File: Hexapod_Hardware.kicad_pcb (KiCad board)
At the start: 4 copper layers, 92.2 x 72.1 mm, 107 parts, among them IC1 MCP3008-I_SL, IC2 MCP3008-I_SL, IC3 MCP3008-I_SL, IC4 STM32G030K8T6, J1 Conn_01x05_Pin, J10 Conn_01x03_Female, J11 Conn_01x03_Female, J12 Conn_01x03_Female, J13 Conn_01x03_Female, J14 Conn_01x03_Female, J15 Conn_01x04_MountingPin, J16 Conn_01x04_MountingPin, J17 Conn_01x04_MountingPin, J18 Screw_Terminal_01x02, J19 Screw_Terminal_01x02, J2 Conn_01x04_Socket, J20 Conn_01x04_Pin, J21 Conn_01x04_Pin, J22 Conn_01x07, J23 Conn_01x03, J3 Conn_01x03_Female, J4 Conn_01x03_Female, J5 Conn_01x03_Female, J6 Conn_01x03_Female, J7 Conn_01x03_Female, J8 Conn_01x03_Female, J9 Conn_01x03_Female, U1 Pico, U10 LM2902, U11 LM2902, U2 LM2902, U3 LM2902, U4 LM2902, U5 LM2902, U6 LM2902, U7 LM2902, U8 AZ1117CH-5.0TRG1

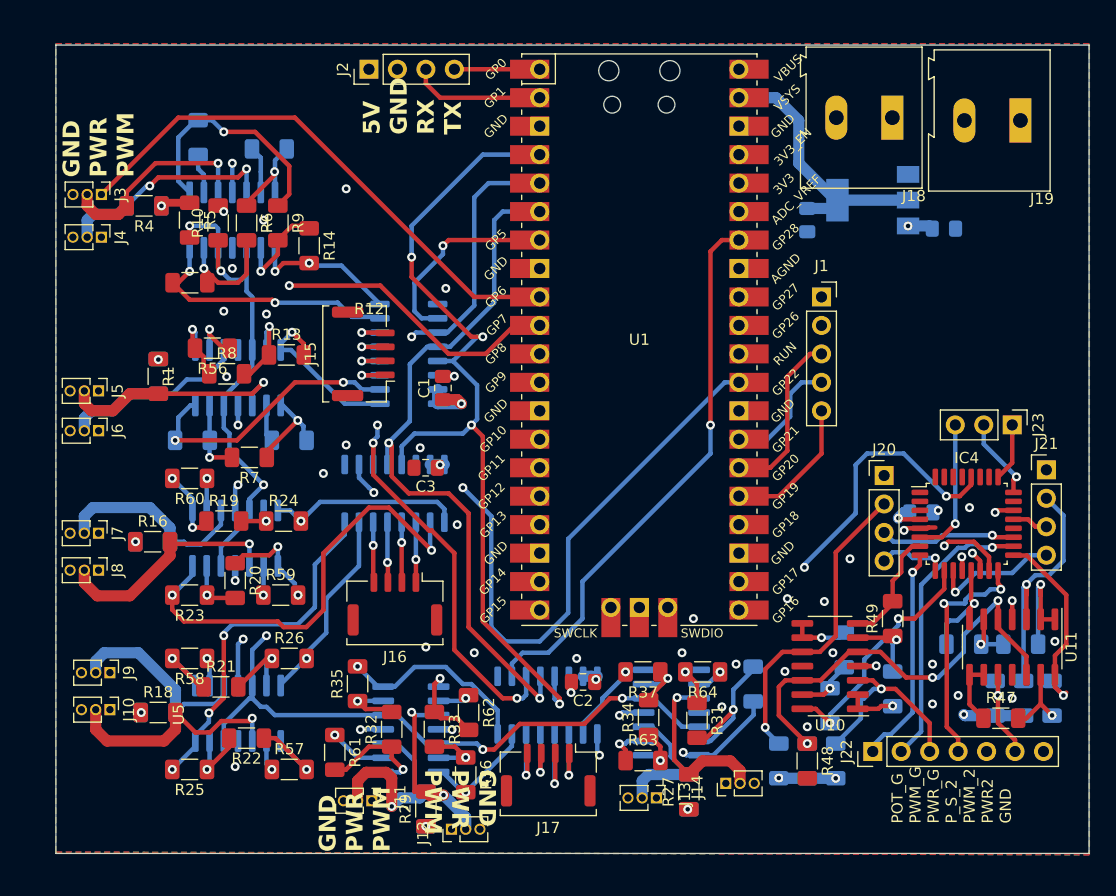
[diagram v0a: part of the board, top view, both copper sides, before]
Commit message: Added testing board + fixed gerber files
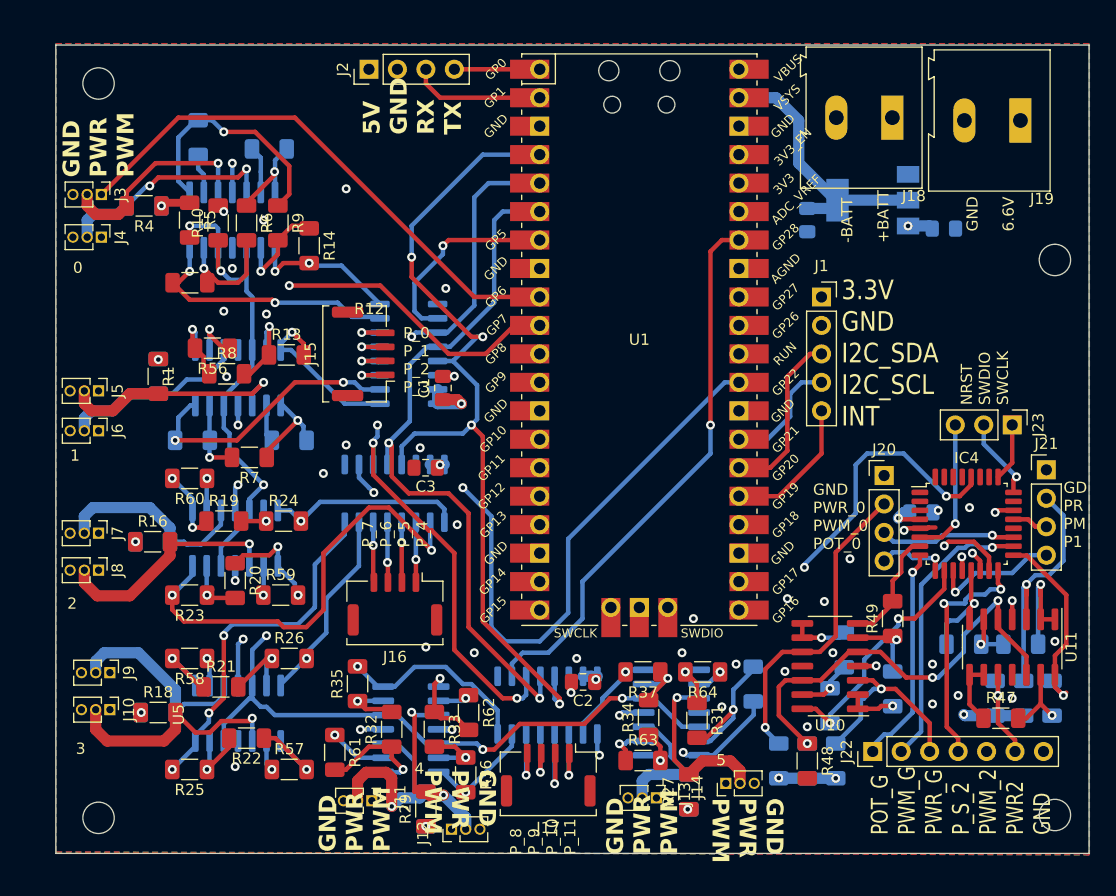
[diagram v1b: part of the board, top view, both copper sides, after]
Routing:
- net +6V: track 209.3 -> 212.5 mm
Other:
- outline, holes or cut-outs redrawn
- board text added: "-BATT +BATT"
- board text added: "0"
- board text added: "1"
- board text added: "2"
- board text added: "3"
- board text added: "3.3V GND I2C_SDA I2C_SCL INT"
- board text added: "4"
- board text added: "5"
- board text added: "GD PR PM P1"
- board text added: "GND 6.6V"
- board text added: "GND PWR_0 PWM_0 POT_0"
- board text added: "NRST SWDIO SWCLK"
- board text added: "P_0 P_1 P_2 P_3"
- board text added: "P_7 P_6 P_5 P_4"
- board text added: "P_8 P_9 P_10 P_11"

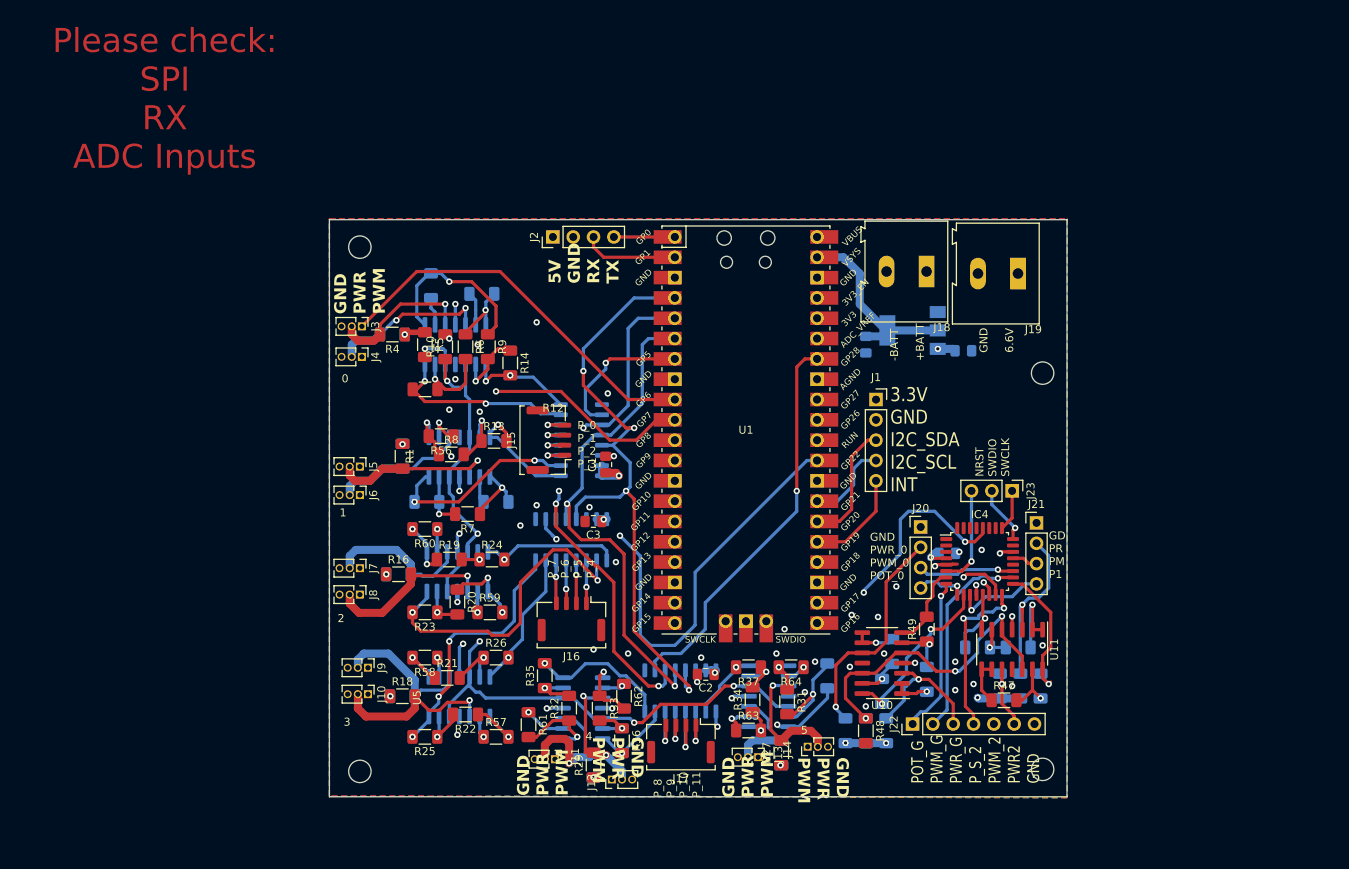
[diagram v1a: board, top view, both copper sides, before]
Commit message: Bord v1.2, added flash memory, changed pinout od servomotor connectors and removed potentiometer signal from servomotors plus one ADC
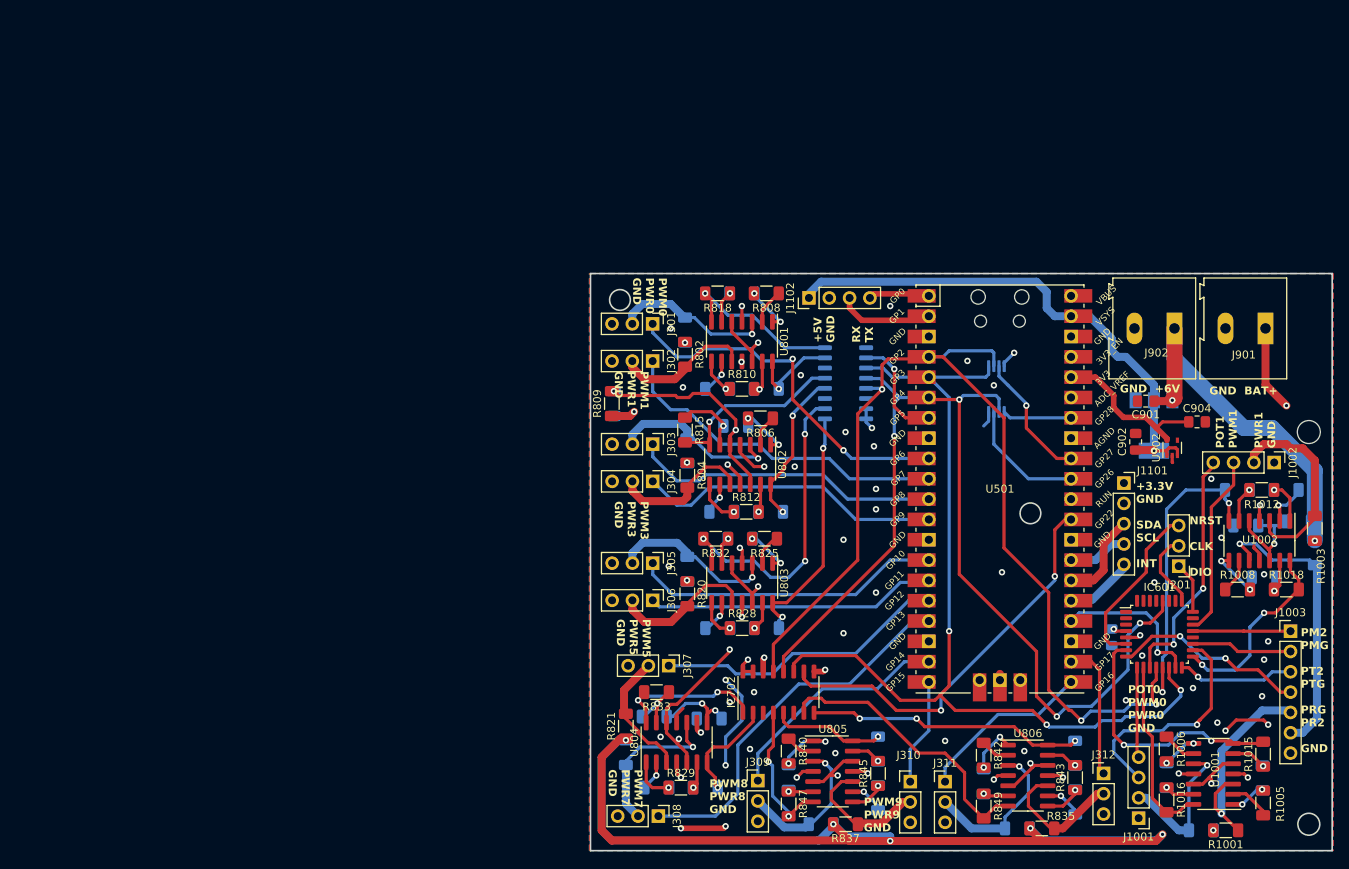
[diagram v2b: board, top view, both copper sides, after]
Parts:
- removed C1, C2, C3: 0,1uF, Capacitor_SMD:C_0805_2012Metric_Pad1.18x1.45mm_HandSolder
- removed C4, C5: 22uF, Capacitor_SMD:C_0805_2012Metric_Pad1.18x1.45mm_HandSolder
- removed C8: 10uF, Capacitor_SMD:C_0805_2012Metric_Pad1.18x1.45mm_HandSolder
- removed IC1, IC2, IC3: MCP3008-I_SL, Package_SO:SO-16_3.9x9.9mm_P1.27mm
- removed IC4: STM32G030K8T6, Package_QFP:LQFP-32_7x7mm_P0.8mm
- removed J1: Conn_01x05_Pin, Connector_PinSocket_2.54mm:PinSocket_1x05_P2.54mm_Vertical
- removed J10, J11, J12, J13, J14, J3, J4, J5, J6, J7, J8, J9: Conn_01x03_Female, Connector_PinHeader_1.27mm:PinHeader_1x03_P1.27mm_Vertical
- removed J15, J16, J17: Conn_01x04_MountingPin, Connector_Molex:Molex_CLIK-Mate_502382-0470_1x04-1MP_P1.25mm_Vertical
- removed J18, J19: Screw_Terminal_01x02, TerminalBlock:TerminalBlock_Altech_AK300-2_P5.00mm
- removed J2: Conn_01x04_Socket, Connector_PinHeader_2.54mm:PinHeader_1x04_P2.54mm_Vertical
- removed J20, J21: Conn_01x04_Pin, Connector_PinHeader_2.54mm:PinHeader_1x04_P2.54mm_Vertical
- removed J22: Conn_01x07, Connector_PinHeader_2.54mm:PinHeader_1x07_P2.54mm_Vertical
- removed J23: Conn_01x03, Connector_PinHeader_2.54mm:PinHeader_1x03_P2.54mm_Vertical
- removed R1, R10, R11, R12, R13, R14, R15, R16, R17, R18, R19, R2, R20, R21, R22, R23, R24, R25, R26, R27, R28, R29, R3, R30, R31, R32, R33, R34, R35, R36, R37, R38, R39, R4, R40, R41, R42, R43, R44, R45, R46, R47, R48, R49, R5, R50, R51, R52, R53, R54, R55, R56, R57, R58, R59, R6, R60, R61, R62, R63, R64, R7, R8, R9: R, Resistor_SMD:R_1206_3216Metric_Pad1.30x1.75mm_HandSolder
- removed U1: Pico, MCU_RaspberryPi_and_Boards:RPi_Pico_SMD_TH
- removed U10, U11, U2, U3, U4, U5, U6, U7: LM2902, Package_SO:SOIC-14_3.9x8.7mm_P1.27mm
- removed U8: AZ1117CH-5.0TRG1, Package_TO_SOT_SMD:SOT-223-3_TabPin2
- added C601: 10uF, Capacitor_SMD:C_0805_2012Metric_Pad1.18x1.45mm_HandSolder, B.Cu at (156.5, 95.2)
- added C901: 22uF, Capacitor_SMD:C_0805_2012Metric_Pad1.18x1.45mm_HandSolder, F.Cu at (160.7, 65.7)
- added C902: 22uF, Capacitor_SMD:C_0805_2012Metric_Pad1.18x1.45mm_HandSolder, F.Cu at (159.5, 70.8)
- added C904: 1uF, Capacitor_SMD:C_0805_2012Metric_Pad1.18x1.45mm_HandSolder, F.Cu at (167.1, 68.3)
- added IC601: STM32G030K8T6, Package_QFP:LQFP-32_7x7mm_P0.8mm, F.Cu at (162.4, 94.9)
- added IC701: MCP3008-I_SL, Package_SO:SO-16_3.9x9.9mm_P1.27mm, B.Cu at (123.2, 63.5)
- added IC702: MCP3008-I_SL, Package_SO:SO-16_3.9x9.9mm_P1.27mm, F.Cu at (114.8, 102.1)
- added J1001: Conn_01x04_Pin, Connector_PinHeader_2.54mm:PinHeader_1x04_P2.54mm_Vertical, F.Cu at (159.8, 117.9)
- added J1002: Conn_01x04_Pin, Connector_PinHeader_2.54mm:PinHeader_1x04_P2.54mm_Vertical, F.Cu at (176.8, 73.4)
- added J1003: Conn_01x07, Connector_PinHeader_2.54mm:PinHeader_1x07_P2.54mm_Vertical, F.Cu at (178.8, 94.5)
- added J1101: Conn_01x05_Pin, Connector_PinSocket_2.54mm:PinSocket_1x05_P2.54mm_Vertical, F.Cu at (158.0, 76.0)
- added J1102: Conn_01x04_Socket, Connector_PinHeader_2.54mm:PinHeader_1x04_P2.54mm_Vertical, F.Cu at (118.6, 52.8)
- added J201: Conn_01x03, Connector_PinHeader_2.54mm:PinHeader_1x03_P2.54mm_Vertical, F.Cu at (164.8, 86.4)
- added J301: Conn_01x03_Female, Connector_PinHeader_2.54mm:PinHeader_1x03_P2.54mm_Vertical, F.Cu at (99.1, 56.1)
- added J302: Conn_01x03_Female, Connector_PinHeader_2.54mm:PinHeader_1x03_P2.54mm_Vertical, F.Cu at (99.1, 60.7)
- added J303: Conn_01x03_Female, Connector_PinHeader_2.54mm:PinHeader_1x03_P2.54mm_Vertical, F.Cu at (99.1, 71.1)
- added J304: Conn_01x03_Female, Connector_PinHeader_2.54mm:PinHeader_1x03_P2.54mm_Vertical, F.Cu at (99.1, 75.8)
- added J305: Conn_01x03_Female, Connector_PinHeader_2.54mm:PinHeader_1x03_P2.54mm_Vertical, F.Cu at (99.1, 86.0)
- added J306: Conn_01x03_Female, Connector_PinHeader_2.54mm:PinHeader_1x03_P2.54mm_Vertical, F.Cu at (99.1, 90.6)
- added J307: Conn_01x03_Female, Connector_PinHeader_2.54mm:PinHeader_1x03_P2.54mm_Vertical, F.Cu at (101.1, 98.8)
- added J308: Conn_01x03_Female, Connector_PinHeader_2.54mm:PinHeader_1x03_P2.54mm_Vertical, F.Cu at (99.8, 117.6)
- added J309: Conn_01x03_Female, Connector_PinHeader_2.54mm:PinHeader_1x03_P2.54mm_Vertical, F.Cu at (112.2, 113.2)
- added J310: Conn_01x03_Female, Connector_PinHeader_2.54mm:PinHeader_1x03_P2.54mm_Vertical, F.Cu at (131.3, 113.3)
- added J311: Conn_01x03_Female, Connector_PinHeader_2.54mm:PinHeader_1x03_P2.54mm_Vertical, F.Cu at (135.6, 113.3)
- added J312: Conn_01x03_Female, Connector_PinHeader_2.54mm:PinHeader_1x03_P2.54mm_Vertical, F.Cu at (155.4, 112.3)
- added J901: Screw_Terminal_01x02, TerminalBlock:TerminalBlock_Altech_AK300-2_P5.00mm, F.Cu at (175.7, 56.6)
- added J902: Screw_Terminal_01x02, TerminalBlock:TerminalBlock_Altech_AK300-2_P5.00mm, F.Cu at (164.3, 56.6)
- added R1001: R, Resistor_SMD:R_1206_3216Metric_Pad1.30x1.75mm_HandSolder, F.Cu at (170.7, 119.4)
- added R1002: R, Resistor_SMD:R_1206_3216Metric_Pad1.30x1.75mm_HandSolder, B.Cu at (167.7, 119.4)
- added R1003: R, Resistor_SMD:R_1206_3216Metric_Pad1.30x1.75mm_HandSolder, F.Cu at (181.9, 81.6)
- added R1004: R, Resistor_SMD:R_1206_3216Metric_Pad1.30x1.75mm_HandSolder, B.Cu at (181.9, 84.7)
- added R1005: R, Resistor_SMD:R_1206_3216Metric_Pad1.30x1.75mm_HandSolder, F.Cu at (175.4, 116.0)
- added R1006: R, Resistor_SMD:R_1206_3216Metric_Pad1.30x1.75mm_HandSolder, F.Cu at (163.3, 109.2)
- added R1007: R, Resistor_SMD:R_1206_3216Metric_Pad1.30x1.75mm_HandSolder, B.Cu at (178.3, 76.8)
- added R1008: R, Resistor_SMD:R_1206_3216Metric_Pad1.30x1.75mm_HandSolder, F.Cu at (172.2, 89.3)
- added R1009: 10k, Resistor_SMD:R_1206_3216Metric_Pad1.30x1.75mm_HandSolder, B.Cu at (179.8, 80.8)
- added R1010: 10k, Resistor_SMD:R_1206_3216Metric_Pad1.30x1.75mm_HandSolder, B.Cu at (175.3, 112.8)
- added R1011: 10k, Resistor_SMD:R_1206_3216Metric_Pad1.30x1.75mm_HandSolder, B.Cu at (163.3, 112.5)
- added R1012: 10k, Resistor_SMD:R_1206_3216Metric_Pad1.30x1.75mm_HandSolder, F.Cu at (175.2, 76.8)
- added R1013: 10k, Resistor_SMD:R_1206_3216Metric_Pad1.30x1.75mm_HandSolder, B.Cu at (175.5, 87.8)
- added R1014: 47k, Resistor_SMD:R_1206_3216Metric_Pad1.30x1.75mm_HandSolder, B.Cu at (173.2, 81.3)
- added R1015: 47k, Resistor_SMD:R_1206_3216Metric_Pad1.30x1.75mm_HandSolder, F.Cu at (175.4, 109.9)
- added R1016: 47k, Resistor_SMD:R_1206_3216Metric_Pad1.30x1.75mm_HandSolder, F.Cu at (163.3, 115.6)
- added R1017: 47k, Resistor_SMD:R_1206_3216Metric_Pad1.30x1.75mm_HandSolder, B.Cu at (172.2, 76.8)
- added R1018: 47k, Resistor_SMD:R_1206_3216Metric_Pad1.30x1.75mm_HandSolder, F.Cu at (178.3, 89.3)
- added R801: 0R39, Resistor_SMD:R_1206_3216Metric_Pad1.30x1.75mm_HandSolder, B.Cu at (103.1, 56.8)
- added R802: R, Resistor_SMD:R_1206_3216Metric_Pad1.30x1.75mm_HandSolder, F.Cu at (103.1, 59.9)
- added R803: R, Resistor_SMD:R_1206_3216Metric_Pad1.30x1.75mm_HandSolder, B.Cu at (103.4, 71.9)
- added R804: R, Resistor_SMD:R_1206_3216Metric_Pad1.30x1.75mm_HandSolder, F.Cu at (103.4, 75.0)
- added R805: R, Resistor_SMD:R_1206_3216Metric_Pad1.30x1.75mm_HandSolder, B.Cu at (107.7, 79.6)
- added R806: R, Resistor_SMD:R_1206_3216Metric_Pad1.30x1.75mm_HandSolder, F.Cu at (112.6, 67.9)
- added R807: R, Resistor_SMD:R_1206_3216Metric_Pad1.30x1.75mm_HandSolder, B.Cu at (107.2, 64.2)
- added R808: R, Resistor_SMD:R_1206_3216Metric_Pad1.30x1.75mm_HandSolder, F.Cu at (113.3, 52.3)
- added R809: 10k, Resistor_SMD:R_1206_3216Metric_Pad1.30x1.75mm_HandSolder, F.Cu at (94.0, 66.0)
- added R810: 10k, Resistor_SMD:R_1206_3216Metric_Pad1.30x1.75mm_HandSolder, F.Cu at (110.2, 64.2)
- added R811: 10k, Resistor_SMD:R_1206_3216Metric_Pad1.30x1.75mm_HandSolder, B.Cu at (109.5, 68.8)
- added R812: 10k, Resistor_SMD:R_1206_3216Metric_Pad1.30x1.75mm_HandSolder, F.Cu at (110.8, 79.6)
- added R813: 10k, Resistor_SMD:R_1206_3216Metric_Pad1.30x1.75mm_HandSolder, B.Cu at (110.2, 52.3)
- added R814: 47k, Resistor_SMD:R_1206_3216Metric_Pad1.30x1.75mm_HandSolder, B.Cu at (94.2, 66.0)
- added R815: 47k, Resistor_SMD:R_1206_3216Metric_Pad1.30x1.75mm_HandSolder, F.Cu at (103.1, 69.3)
- added R816: 47k, Resistor_SMD:R_1206_3216Metric_Pad1.30x1.75mm_HandSolder, B.Cu at (113.3, 64.2)
- added R817: 47k, Resistor_SMD:R_1206_3216Metric_Pad1.30x1.75mm_HandSolder, B.Cu at (113.8, 79.6)
- added R818: 47k, Resistor_SMD:R_1206_3216Metric_Pad1.30x1.75mm_HandSolder, F.Cu at (107.2, 52.3)
- added R819: R, Resistor_SMD:R_1206_3216Metric_Pad1.30x1.75mm_HandSolder, B.Cu at (103.4, 86.7)
- added R820: R, Resistor_SMD:R_1206_3216Metric_Pad1.30x1.75mm_HandSolder, F.Cu at (103.4, 89.8)
- added R821: R, Resistor_SMD:R_1206_3216Metric_Pad1.30x1.75mm_HandSolder, F.Cu at (95.7, 106.4)
- added R822: R, Resistor_SMD:R_1206_3216Metric_Pad1.30x1.75mm_HandSolder, B.Cu at (95.7, 109.7)
- added R823: R, Resistor_SMD:R_1206_3216Metric_Pad1.30x1.75mm_HandSolder, B.Cu at (106.1, 105.4)
- added R824: R, Resistor_SMD:R_1206_3216Metric_Pad1.30x1.75mm_HandSolder, B.Cu at (107.2, 94.1)
- added R825: R, Resistor_SMD:R_1206_3216Metric_Pad1.30x1.75mm_HandSolder, F.Cu at (113.1, 82.9)
- added R826: R, Resistor_SMD:R_1206_3216Metric_Pad1.30x1.75mm_HandSolder, B.Cu at (99.6, 114.0)
- added R827: 10k, Resistor_SMD:R_1206_3216Metric_Pad1.30x1.75mm_HandSolder, B.Cu at (110.0, 82.9)
- added R828: 10k, Resistor_SMD:R_1206_3216Metric_Pad1.30x1.75mm_HandSolder, F.Cu at (110.3, 94.1)
- added R829: 10k, Resistor_SMD:R_1206_3216Metric_Pad1.30x1.75mm_HandSolder, F.Cu at (102.6, 114.0)
- added R830: 10k, Resistor_SMD:R_1206_3216Metric_Pad1.30x1.75mm_HandSolder, B.Cu at (99.3, 105.2)
- added R831: 47k, Resistor_SMD:R_1206_3216Metric_Pad1.30x1.75mm_HandSolder, B.Cu at (113.3, 94.1)
- added R832: 47k, Resistor_SMD:R_1206_3216Metric_Pad1.30x1.75mm_HandSolder, F.Cu at (107.0, 82.9)
- added R833: 47k, Resistor_SMD:R_1206_3216Metric_Pad1.30x1.75mm_HandSolder, F.Cu at (99.6, 102.1)
- added R834: 47k, Resistor_SMD:R_1206_3216Metric_Pad1.30x1.75mm_HandSolder, B.Cu at (105.7, 114.0)
- added R835: R, Resistor_SMD:R_1206_3216Metric_Pad1.30x1.75mm_HandSolder, F.Cu at (147.7, 119.1)
- added R836: R, Resistor_SMD:R_1206_3216Metric_Pad1.30x1.75mm_HandSolder, B.Cu at (120.1, 118.6)
- added R837: R, Resistor_SMD:R_1206_3216Metric_Pad1.30x1.75mm_HandSolder, F.Cu at (123.2, 118.6)
- added R838: R, Resistor_SMD:R_1206_3216Metric_Pad1.30x1.75mm_HandSolder, B.Cu at (144.7, 119.1)
- added R839: R, Resistor_SMD:R_1206_3216Metric_Pad1.30x1.75mm_HandSolder, B.Cu at (151.9, 115.8)
- added R840: R, Resistor_SMD:R_1206_3216Metric_Pad1.30x1.75mm_HandSolder, F.Cu at (116.1, 109.5)
- added R841: 47k, Resistor_SMD:R_1206_3216Metric_Pad1.30x1.75mm_HandSolder, B.Cu at (127.3, 115.3)
- added R842: R, Resistor_SMD:R_1206_3216Metric_Pad1.30x1.75mm_HandSolder, F.Cu at (140.5, 110.0)
- added R843: 10k, Resistor_SMD:R_1206_3216Metric_Pad1.30x1.75mm_HandSolder, F.Cu at (151.9, 112.8)
- added R844: 10k, Resistor_SMD:R_1206_3216Metric_Pad1.30x1.75mm_HandSolder, B.Cu at (116.1, 112.8)
- added R845: 10k, Resistor_SMD:R_1206_3216Metric_Pad1.30x1.75mm_HandSolder, F.Cu at (127.3, 112.3)
- added R846: 10k, Resistor_SMD:R_1206_3216Metric_Pad1.30x1.75mm_HandSolder, B.Cu at (140.5, 113.3)
- added R847: 47k, Resistor_SMD:R_1206_3216Metric_Pad1.30x1.75mm_HandSolder, F.Cu at (116.1, 116.1)
- added R848: 47k, Resistor_SMD:R_1206_3216Metric_Pad1.30x1.75mm_HandSolder, B.Cu at (127.3, 109.2)
- added R849: 47k, Resistor_SMD:R_1206_3216Metric_Pad1.30x1.75mm_HandSolder, F.Cu at (140.5, 116.3)
- added R850: 47k, Resistor_SMD:R_1206_3216Metric_Pad1.30x1.75mm_HandSolder, B.Cu at (151.9, 109.7)
- added U1001: LM2902, Package_SO:SOIC-14_3.9x8.7mm_P1.27mm, F.Cu at (169.2, 112.3)
- added U1002: LM2902, Package_SO:SOIC-14_3.9x8.7mm_P1.27mm, F.Cu at (174.9, 83.2)
- added U1101: AT25SF081-XMHD-X, Package_SO:TSSOP-8_4.4x3mm_P0.65mm, B.Cu at (142.1, 64.2)
- added U501: Pico, MCU_RaspberryPi_and_Boards:RPi_Pico_SMD_TH, F.Cu at (142.5, 76.7)
- added U801: LM2902, Package_SO:SOIC-14_3.9x8.7mm_P1.27mm, F.Cu at (110.2, 58.3)
- added U802: LM2902, Package_SO:SOIC-14_3.9x8.7mm_P1.27mm, F.Cu at (110.0, 73.7)
- added U803: LM2902, Package_SO:SOIC-14_3.9x8.7mm_P1.27mm, F.Cu at (110.3, 88.5)
- added U804: LM2902, Package_SO:SOIC-14_3.9x8.7mm_P1.27mm, F.Cu at (102.1, 108.4)
- added U805: LM2902, Package_SO:SOIC-14_3.9x8.7mm_P1.27mm, F.Cu at (121.6, 112.0)
- added U806: LM2902, Package_SO:SOIC-14_3.9x8.7mm_P1.27mm, F.Cu at (146.0, 112.5)
- added U901: AZ1117CH-5.0TRG1, Package_TO_SOT_SMD:SOT-223-3_TabPin2, B.Cu at (161.7, 68.8)
- added U902: LD29150DT33R, Package_TO_SOT_SMD:SOT-353_SC-70-5, F.Cu at (164.0, 71.6)
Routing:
- net /MCU/SPI_CLK: track 0.00 -> 132.3 mm, vias 0 -> 3
- net /MCU/SPI_MISO: track 0.00 -> 127.2 mm, vias 0 -> 4
- net /Gripper/SPI_SCK: track 127.1 -> 0.00 mm, vias 6 -> 0
- net /Gripper/SPI_MOSI: track 121.6 -> 0.00 mm, vias 7 -> 0
- net /Gripper/SPI_MISO: track 120.2 -> 0.00 mm, vias 5 -> 0
- net /MCU/SPI_MOSI: track 0.00 -> 118.0 mm, vias 0 -> 3
- net +6V: track 212.5 -> 329.9 mm, vias 10 -> 12
- net /SERVO + ADC/Current Sensors/V_BAT_REF: track 116.9 -> 204.8 mm, vias 6 -> 8
- net +5V: track 142.9 -> 66.3 mm, vias 0 -> 1
- net +8V: track 197.7 -> 258.7 mm, vias 8 -> 9
- net /SUPPORTING_MODULES/Gripper/Gripper_servo/V_BAT_REF: track 0.00 -> 57.1 mm, vias 0 -> 4
- net /MCU/SPI_CS_2: track 49.6 -> 8.66 mm, vias 1 -> 0
- net /Gripper/Gripper_servo/V_BAT_REF: track 39.3 -> 0.00 mm, vias 3 -> 0
- net /SUPPORTING_MODULES/Gripper/Gripper_servo/SERVO_1_CURRENT: track 0.00 -> 38.5 mm, vias 0 -> 2
- net +3.3V: track 11.2 -> 48.2 mm, vias 4 -> 8
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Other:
- board size 92.2 x 72.1 mm -> 92.7 x 72.1 mm
- board text added: "+3.3V GND SDA SCL INT"
- board text added: "+5V GND RX TX"
- board text added: "GND +6V"
- board text added: "GND BAT+"
- board text added: "NRST CLK DIO"
- board text added: "PM2 PMG PT2 PTG PRG PR2 GND"
- board text added: "POT0 PWM0 PWR0 GND"
- board text added: "POT1 PWM1 PWR1 GND"
- board text added: "PWM0 PWR0 GND"
- board text added: "PWM1 PWR1 GND"
- board text added: "PWM3 PWR3 GND"
- board text added: "PWM5 PWR5 GND"
- board text added: "PWM7 PWR7 GND"
- board text added: "PWM8 PWR8 GND"
- board text added: "PWM9 PWR9 GND"
- board text removed: "-BATT +BATT"
- board text removed: "0"
- board text removed: "1"
- board text removed: "2"
- board text removed: "3"
- board text removed: "3.3V GND I2C_SDA I2C_SCL INT"
- board text removed: "4"
- board text removed: "5"
- board text removed: "5V GND RX TX"
- board text removed: "GD PR PM P1"
- board text removed: "GND 6.6V"
- board text removed: "GND PWR PWM"
- board text removed: "GND PWR_0 PWM_0 POT_0"
- board text removed: "NRST SWDIO SWCLK"
- board text removed: "POT_G PWM_G PWR_G P_S_2 PWM_2 PWR2 GND"
- board text removed: "P_0 P_1 P_2 P_3"
- board text removed: "P_7 P_6 P_5 P_4"
- board text removed: "P_8 P_9 P_10 P_11"
- board text removed: "Please check: SPI RX ADC Inputs"

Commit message: new pcb
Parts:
- U1101: footprint Package_SO:TSSOP-8_4.4x3mm_P0.65mm -> Package_SO:SOP-8_3.9x4.9mm_P1.27mm
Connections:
- IC701 pad 3: unconnected-(IC701-CH2-Pad3) -> Net-(IC701-CH2)
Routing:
- net /MCU/FLASH_HOLD: track 16.3 -> 18.7 mm, vias 1 -> 2
- net GND: track 22.1 -> 20.1 mm
- net /MCU/SPI_MOSI: track 118.0 -> 116.4 mm
- net /MCU/SPI_CS_2: track 8.66 -> 7.83 mm
- net +3.3V: track 48.2 -> 49.0 mm
